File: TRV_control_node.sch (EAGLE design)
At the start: 47 parts, among them J1 AMP FCI 10103594-0001LF, J3 USB-MICROB, J4 455-1750-1-ND, J6 AMP FCI 10103594-0001LF, Q6 BSS84W-7-F, SW1 EVQQ, SW2 EVQQ, U1 PCA9306, U11 915MHz, U2 FT231XQ-R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

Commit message: schematic changes
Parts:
- removed J2: (no value), SparkFun-Connectors:CONN_04
- removed Q6: BSS84W-7-F, MOSFETs:MOSFET-PCH-BSS84W
- removed R13, R6: 10K, Adafruit Feather 32u4 Bluefruit LE:MICROBUILDER_RESISTOR_0402MP
- removed R21: 10M, Adafruit Feather 32u4 Bluefruit LE:MICROBUILDER_RESISTOR_0402MP
- added C3: 100uF, adafruit:C-USC1210
- added C7: 0.1uF, Adafruit Feather 32u4 Bluefruit LE:MICROBUILDER_CAP_CERAMIC_0402MP
- added J5: AMP FCI 10103594-0001LF, SparkFun-Connectors:USB_MICRO-B_HALF_PTH
- added U$1: OLED_091_SSD1306, oled_096_SSD1306:OLED_091_SSD1306
- J3: value USB-MICROB -> AMP FCI 10103594-0001LF; device SparkFun-Connectors:USB-MICROB -> SparkFun-Connectors:USB_MICRO-B_HALF_PTH; MPN ZX62-B-5PA(33) -> (none)
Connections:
- removed net 5.0V: RPI1.5.0V, RPI1.5.0V@1
- removed net D+: J6.D+
- removed net D-: J6.D-
- removed net FTDI_RX: R20.1
- removed net GND1: J6.GND
- removed net VBAT: Q6.D1
- new net 5VA: C6.2, D2.A, J1.VBUS, J6.VBUS, RPI1.5.0V, RPI1.5.0V@1, U2.VCC
- net 3.3V: no longer RPI1.3.3V, RPI1.3.3V@1
- net 3.3VB: now also RPI1.3.3V, RPI1.3.3V@1, U$1.VCC
- net 5VB: now also C3.1, C7.2, J3.VBUS, J4.3, J5.VBUS
- net CH0: now also J4.2
- net GND: now also C3.2, C7.1, J1.GND, J4.1, J5.GND, J6.GND, U$1.GND; no longer R21.1
- net N$32: now also J1.D-, J6.D-; no longer J3.D-
- net N$33: now also J1.D+, J6.D+; no longer J3.D+
- net RX: now also RPI1.TXD
- net SCL: now also U$1.SCL; no longer R13.1
- net SDA: now also U$1.SDA; no longer R6.1
- net TX: now also R20.1, RPI1.RXD
- net VBUS: no longer C6.2, D2.A, J3.VBUS, J6.VBUS, Q6.G1, R21.2, U2.VCC
- net VCC: no longer R13.2, R6.2
- net VIN: no longer Q6.S1
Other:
- note added: "OLED screen"
- note added: "Servo"
- note added: "Servo Controller"
- moved on the sheet: C1, C6, D2, J1, J4, J6, R11, R15, R17, R18, R19, R20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

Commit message: Arranged components on brd
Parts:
- removed C2: 10uF, microbuilder:CAP_CERAMIC0805-NOOUTLINE
- removed C4: 10uF, SparkFun-Capacitors:CAP0805
- removed J1, J5: AMP FCI 10103594-0001LF, SparkFun-Connectors:USB_MICRO-B_HALF_PTH
- removed R1, R2: 10k, SparkFun-Resistors:10KOHM-0603-1/10W-1%
- removed R4: 200k, SparkFun-Resistors:200KOHM-0603-1/10W-1%
- added C10: 1uF, Adafruit Feather 32u4 Bluefruit LE:MICROBUILDER_CAP_CERAMIC_0402MP
- added C8: 10uF, Adafruit Feather 32u4 Bluefruit LE:MICROBUILDER_CAP_CERAMIC_0402MP
- added R10, R6: 10K, Adafruit Feather 32u4 Bluefruit LE:MICROBUILDER_RESISTOR_0402MP
- added R12: 200K, Adafruit Feather 32u4 Bluefruit LE:MICROBUILDER_RESISTOR_0402MP
- added U$3: OLED_091_SSD1306, oled_096_SSD1306:OLED_091_SSD1306
- C1: value 1uF -> 10uF; device SparkFun-Capacitors:CAP0805 -> Adafruit Feather 32u4 Bluefruit LE:MICROBUILDER_CAP_CERAMIC_0402MP; MPN CC0805ZRY5V8BB105 -> GRM155R71C104KA88J
- R7, R8: value 10k -> 10K; device SparkFun-Resistors:10KOHM-0603-1/10W-1% -> Adafruit Feather 32u4 Bluefruit LE:MICROBUILDER_RESISTOR_0402MP; MPN (none) -> RC0402JR-071KL
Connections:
- removed net 3.3V: C2.1
- net 3.3VB: now also C1.2, R10.1, R6.1; no longer R7.2, R8.2
- net 5VA: no longer J1.VBUS
- net 5VB: now also R12.1, R7.1, R8.1; no longer J5.VBUS, R1.2, R2.2, R4.2
- net GND: now also C1.1, C10.1, C8.1; no longer C1.2, C2.2, C4.2, J1.GND, J5.GND
- net LV_SCL: now also R10.2; no longer R7.1
- net LV_SDA: now also R6.2; no longer R8.1
- net N$1: now also R12.2; no longer R4.1
- net N$32: no longer J1.D-
- net N$33: no longer J1.D+
- net N$6: now also R8.2; no longer R2.1
- net N$7: now also R7.2; no longer R1.1
- net SCL: no longer U5.PC5
- net SDA: no longer U5.PC4
- net VCC: now also C8.2; no longer C4.1
- net VIN: now also C10.2; no longer C1.1
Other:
- moved on the sheet: C1, J6

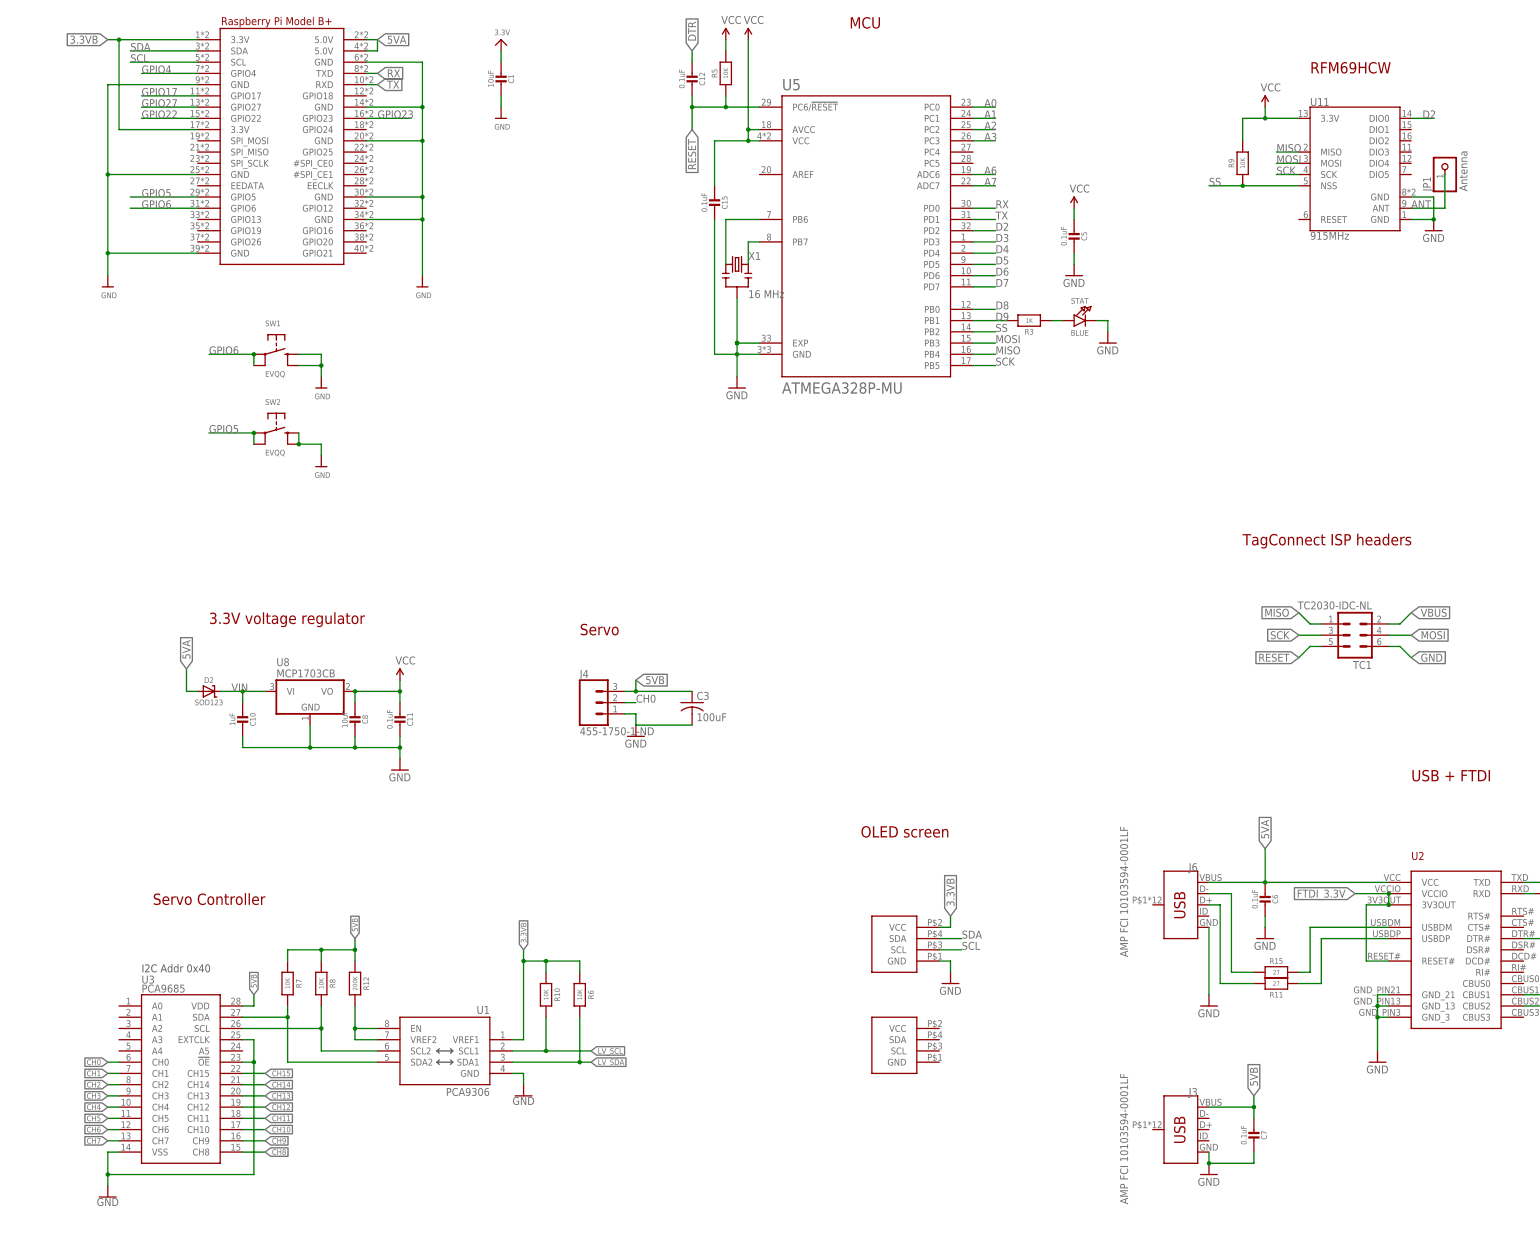
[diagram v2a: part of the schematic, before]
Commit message: Completed routing
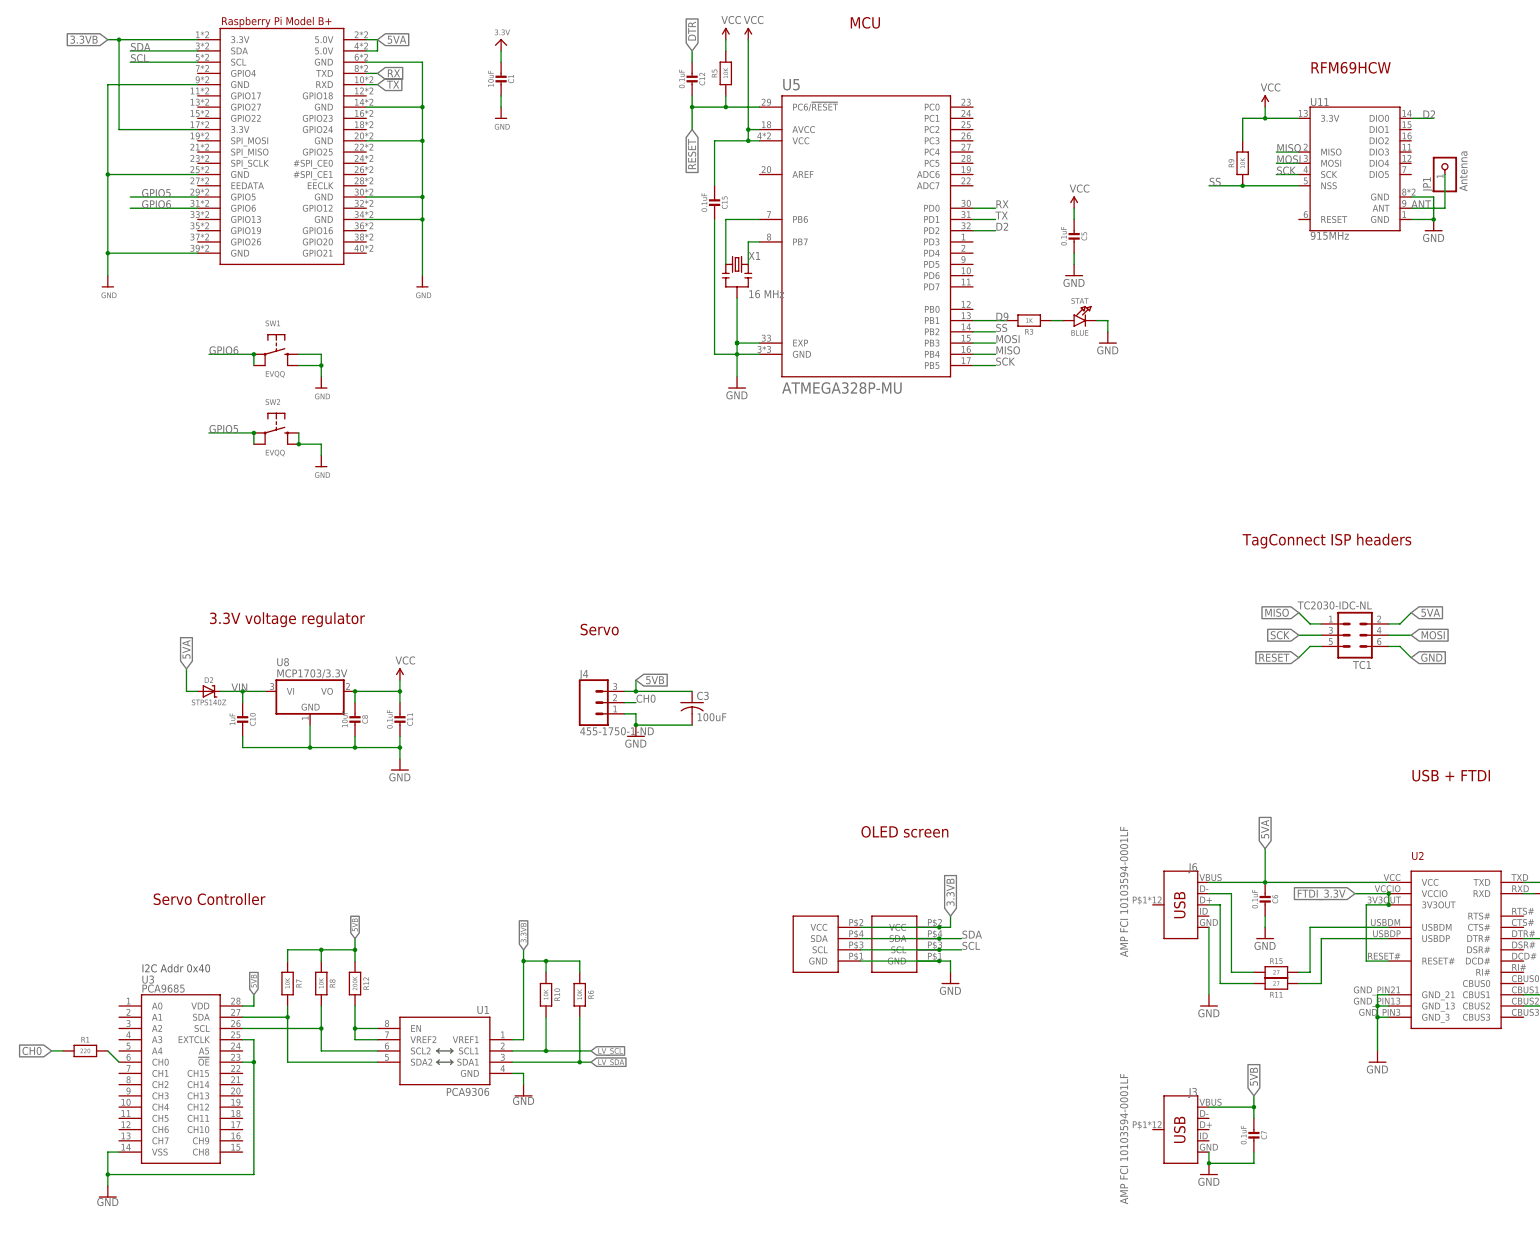
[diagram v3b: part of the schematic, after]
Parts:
- added R1: 220, Adafruit Feather 32u4 Bluefruit LE:MICROBUILDER_RESISTOR_0402MP
- D2: value SOD123 -> STPS140Z
- U8: value MCP1703CB -> MCP1703/3.3V
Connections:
- removed net A0: U5.PC0
- removed net A1: U5.PC1
- removed net A2: U5.PC2
- removed net A3: U5.PC3
- removed net A6: U5.ADC6
- removed net A7: U5.ADC7
- removed net CH1: U3.CH1
- removed net CH10: U3.CH10
- removed net CH11: U3.CH11
- removed net CH12: U3.CH12
- removed net CH13: U3.CH13
- removed net CH14: U3.CH14
- removed net CH15: U3.CH15
- removed net CH2: U3.CH2
- removed net CH3: U3.CH3
- removed net CH4: U3.CH4
- removed net CH5: U3.CH5
- removed net CH6: U3.CH6
- removed net CH7: U3.CH7
- removed net CH8: U3.CH8
- removed net CH9: U3.CH9
- removed net D3: U5.PD3
- removed net D4: U5.PD4
- removed net D5: U5.PD5
- removed net D6: U5.PD6
- removed net D7: U5.PD7
- removed net D8: U5.PB0
- removed net GPIO17: RPI1.GPIO17
- removed net GPIO22: RPI1.GPIO22
- removed net GPIO23: RPI1.GPIO23
- removed net GPIO27: RPI1.GPIO27
- removed net GPIO4: RPI1.GPIO4
- removed net VBUS: TC1.2
- new net N$9: R1.2, U3.CH0
- net 3.3VB: now also U$3.VCC
- net 5VA: now also TC1.2
- net CH0: now also R1.1; no longer U3.CH0
- net GND: now also U$3.GND
- net SCL: now also U$3.SCL
- net SDA: now also U$3.SDA

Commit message: Adjustments
- Removed second OLED screen pins
- Moved USB ports slightly away from each other
- Silkscreen adjustments
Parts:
- removed U$3: OLED_091_SSD1306, oled_096_SSD1306:OLED_091_SSD1306
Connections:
- net 3.3VB: no longer U$3.VCC
- net GND: no longer U$3.GND
- net SCL: no longer U$3.SCL
- net SDA: no longer U$3.SDA
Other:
- note added: "Buttons"
- moved on the sheet: C10, C11, C3, C6, C7, C8, D2, J3, J4, J6, JP1, R1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
